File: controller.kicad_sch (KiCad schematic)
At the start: 26 parts, among them J5 Conn_01x10_Pin, J6 Conn_01x10_Pin, J8 AVR-ISP-6, Q1 BSS138, Q2 BSS138, Q3 BSS138, U10 ATmega328PB-A, Y1 16M

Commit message: weiter layoutet...
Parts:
- removed C14: 27p, symbol Device:C_Small
- removed J6: Conn_01x10_Pin, symbol Connector:Conn_01x10_Pin
- removed Q1, Q2, Q3: BSS138, Package_TO_SOT_SMD:SOT-23, symbol Transistor_FET:BSS138
- removed R11, R5, R7, R8: 1k, symbol Device:R_Small
- removed Y1: 16M, Crystal:Crystal_SMD_HC49-SD, symbol Device:Crystal_Small
- added C37, C46: 2u2, Capacitor_SMD:C_0805_2012Metric_Pad1.18x1.45mm_HandSolder, symbol Device:C_Small
- added C38, C39, C40: 100n, Capacitor_SMD:C_0805_2012Metric_Pad1.18x1.45mm_HandSolder, symbol Device:C_Small
- added D2: LED_Small, LED_SMD:LED_0805_2012Metric_Pad1.15x1.40mm_HandSolder, symbol Device:LED_Small
- added D6: SMAJ5.0CA, Diode_SMD:D_SMA, symbol Diode:SMAJ5.0CA
- added FB5, FB6: FerriteBead_Small, Inductor_SMD:L_0805_2012Metric_Pad1.15x1.40mm_HandSolder, symbol Device:FerriteBead_Small
- added FL1: Choke_Coilcraft_0603USB-251, Inductor_SMD:L_CommonModeChoke_Coilcraft_0603USB, symbol Filter:Choke_Coilcraft_0603USB-251
- added J10: Conn_01x06_Socket, Connector_PinHeader_2.54mm:PinHeader_1x06_P2.54mm_Vertical, symbol Connector:Conn_01x06_Socket
- added J6: Conn_01x06_Socket, Connector_PinHeader_2.54mm:PinHeader_1x06_P2.54mm_Horizontal, symbol Connector:Conn_01x06_Socket
- added J7: USB_B, Connector_USB:USB_B_Lumberg_2411_02_Horizontal, symbol Connector:USB_B
- added R14, R15: 33, Resistor_SMD:R_0805_2012Metric_Pad1.20x1.40mm_HandSolder, symbol Device:R_Small
- added SW1: SW_SP5T_NR01105, Button_Switch_THT:SW_NKK_NR01, symbol Switch:SW_SP5T_NR01105
- added U11: FT232RL, Package_SO:SSOP-28_5.3x10.2mm_P0.65mm, symbol Interface_USB:FT232RL
- added U12: WE-TVS-82400102, Package_TO_SOT_SMD:SOT-23-6, symbol Power_Protection:WE-TVS-82400102
- added Y1: ECS-2520MV-xxx-xx, Oscillator:Oscillator_SMD_ECS_2520MV-xxx-xx-4Pin_2.5x2.0mm, symbol Oscillator:ECS-2520MV-xxx-xx
- C12, C15, C16, C17, C18: footprint (none) -> Capacitor_SMD:C_0805_2012Metric_Pad1.18x1.45mm_HandSolder
- C13: value 27p -> 100n; footprint (none) -> Capacitor_SMD:C_0805_2012Metric_Pad1.18x1.45mm_HandSolder
- FB3: footprint Inductor_SMD:L_0805_2012Metric_Pad1.05x1.20mm_HandSolder -> Inductor_SMD:L_0805_2012Metric_Pad1.15x1.40mm_HandSolder
- J5: footprint (none) -> Connector_PinHeader_2.54mm:PinHeader_1x10_P2.54mm_Vertical
- J8: footprint Connector_IDC:IDC-Header_2x05_P2.54mm_Vertical -> Connector_IDC:IDC-Header_2x03_P2.54mm_Vertical
- R10, R6, R9: footprint (none) -> Resistor_SMD:R_0805_2012Metric_Pad1.20x1.40mm_HandSolder
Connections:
- net SDA_5 is gone; now on net SDA_3: TP1.1, U10.27 (PC4)
- net +3V3: now also FB3.1, J5.10 (Pin_10), J5.9 (Pin_9), J8.2 (VCC)
- net GND: now also C37.1, C38.1, C39.1, C40.1, C46.1, D2.1 (K), D6.1 (A1), J7.4 (GND), J7.5 (Shield), SW1.MP, U11.18 (GND), U11.21 (GND), U11.25 (AGND), U11.7 (GND), U12.2, Y1.1 (Tri-State), Y1.2 (GND)
- net INT_3: now also TP3.1, U10.26 (PC3)
- net RXD: now also U11.5 (RXD)
- net SCL_3: now also TP2.1, U10.28 (PC5)
- net TXD: now also U11.1 (TXD)
- net at U10.8 (XTAL2/PB7): no longer C13.2
- net at U10.1 (PD3): now also J10.2 (Pin_2), J6.2 (Pin_2), SW1.5
- net at U10.10 (PD6): now also J10.5 (Pin_5), J6.5 (Pin_5), SW1.2
- net at U10.11 (PD7): now also J10.6 (Pin_6), J6.6 (Pin_6), SW1.1
- net at U10.2 (PD4): now also J10.3 (Pin_3), J6.3 (Pin_3), SW1.4
- net at U10.3 (PE0): now also R9.2
- net at U10.32 (PD2): now also R10.1
- net at U10.7 (XTAL1/PB6): now also Y1.3 (OUT)
- net at U10.9 (PD5): now also J10.4 (Pin_4), J6.4 (Pin_4), SW1.3
- removed net +5VD: FB3.1, J5.10 (Pin_10), J5.9 (Pin_9), J8.2 (VCC), R10.1, R6.2, R9.1
- net 5VD_FIL renamed 3V3D_FIL
- net 3V3D_FIL: now also C13.2, R6.2, Y1.4 (VDD)
- removed net INT_5: R10.2, TP3.1, U10.26 (PC3)
- removed net SCL_5: R9.2, TP2.1, U10.28 (PC5)
- new net: FB6.1, J7.1 (VBUS)
- new net: FL1.4, J7.2 (D-)
- new net: FL1.1, J7.3 (D+)
- new net: FL1.3, U12.1
- new net: FL1.2, U12.3
- new net: J10.1 (Pin_1), J6.1 (Pin_1), R10.2, SW1.C (Common)
- new net: R15.2, U11.15 (USBD+)
- new net: R14.2, U11.16 (USBD-)
- new net: C39.2, C40.2, U11.17 (3V3OUT), U11.4 (VCCIO)
- new net: D2.2 (A), R9.1
- new net USB_D+: R15.1, U12.4
- new net USB_D-: R14.1, U12.6
- new net VBUS: C46.2, D6.2 (A2), FB5.1, FB6.2, U12.5
- new net VBUS_FIL: C37.2, C38.2, FB5.2, U11.19 (~{RESET}), U11.20 (VCC)
- no-connect marks 7 -> 21
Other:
- moved on the sheet: C12, C15, C16, C17, C18, J5, J8, R6, TP1, TP2, TP3, U10

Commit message: noch ein paar Kleinigkeiten
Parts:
- added C14, C51, C52, C53, C54: 100n, Capacitor_SMD:C_0805_2012Metric_Pad1.18x1.45mm_HandSolder, symbol Device:C_Small
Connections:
- net GND: now also C14.1, C51.1, C52.1, C53.1, C54.1
- net at J10.2 (Pin_2), J6.2 (Pin_2), SW1.5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: now also C54.2
- net at J10.5 (Pin_5), J6.5 (Pin_5), SW1.2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: now also C51.2
- net at J10.6 (Pin_6), J6.6 (Pin_6), SW1.1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: now also C14.2
- net at J10.3 (Pin_3), J6.3 (Pin_3), SW1.4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: now also C53.2
- net at J10.4 (Pin_4), J6.4 (Pin_4), SW1.3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: now also C52.2

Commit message: BOM angefangen und im Layout vom Hundertsten ins Tausendste gekommen...
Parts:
- C12, C13, C14, C15, C16, C38, C39, C40, C51, C52, C53, C54: Distributor (none) -> Mouser; Distributor PN (none) -> 581-KAM21BR71H104JT; Manufacturer (none) -> KYOCERA AVX; Manufacturer PN (none) -> KAM21BR71H104JT
- C17, C18, C37, C46: Distributor (none) -> Mouser; Distributor PN (none) -> 581-KAM21KR71E225KU; Manufacturer (none) -> KYOCERA AVX; Manufacturer PN (none) -> KAM21KR71E225KU
- D2: Distributor (none) -> Mouser; Distributor PN (none) -> 859-LTST-C171KGKT; Manufacturer (none) -> LITEON; Manufacturer PN (none) -> LTST-C171KGKT
- D6: Distributor (none) -> Mouser; Distributor PN (none) -> 576-SMAJ5.0CA; Manufacturer (none) -> Littelfuse; Manufacturer PN (none) -> SMAJ5.0CA
- FL1: Distributor (none) -> Mouser; Distributor PN (none) -> 994-0603USB-601MLC; Manufacturer (none) -> Coilcraft; Manufacturer PN (none) -> 0603USB-601MLC
- J5: now not fitted
- J7: Distributor PN (none) -> 200-USBBSFBTHFR; Manufacturer (none) -> Samtec; Manufacturer PN (none) -> USB-B-S-F-B-TH-FR
- J8: Distributor (none) -> Mouser; Distributor PN (none) -> 737-BHR-06-VUA; Manufacturer (none) -> Adam Tech; Manufacturer PN (none) -> BHR-06-VUA
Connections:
- net at C53.2, J10.3 (Pin_3), J6.3 (Pin_3)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: now also SW1.1; no longer SW1.4
- net at C14.2, J10.6 (Pin_6), J6.6 (Pin_6)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: now also SW1.3; no longer SW1.1
- net at C52.2, J10.4 (Pin_4), J6.4 (Pin_4)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: now also SW1.4; no longer SW1.3
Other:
- moved on the sheet: SW1

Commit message: es wird nicht besser... Beschriftungen und co. BOM angefangen...
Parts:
- added D5, D7: LED_Small, LED_SMD:LED_0805_2012Metric_Pad1.15x1.40mm_HandSolder, symbol Device:LED_Small
- added R11, R16: 1k, Resistor_SMD:R_0805_2012Metric_Pad1.20x1.40mm_HandSolder, symbol Device:R_Small
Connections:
- net GND: now also D5.1 (K), D7.1 (K)
- net at U11.22 (CBUS1): now also R16.2
- net at U11.23 (CBUS0): now also R11.2
- new net: D7.2 (A), R16.1
- new net: D5.2 (A), R11.1
- no-connect marks 21 -> 19

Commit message: BOM...
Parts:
- J10: Distributor (none) -> Mouser; Distributor PN (none) -> TC33X-2-103E; Manufacturer (none) -> Adam Tech; Manufacturer PN (none) -> PH1RB-06-UA
- J7: Distributor (none) -> Mouser
- SW1: Distributor (none) -> Mouser; Distributor PN (none) -> 633-NR01105ANG13-2A; Manufacturer (none) -> NKK Switches; Manufacturer PN (none) -> NR01105ANG13-2A
- U10: Distributor (none) -> Mouser; Distributor PN (none) -> 556-ATMEGA328PB-ANR; Manufacturer (none) -> Microchip Technology; Manufacturer PN (none) -> ATMEGA328PB-ANR
- U11: Distributor (none) -> Mouser; Distributor PN (none) -> 895-FT232RNL-TUBE; Manufacturer (none) -> FTDI; Manufacturer PN (none) -> FT232RNL-TUBE
- U12: Distributor (none) -> Mouser; Distributor PN (none) -> 710-82400102; Manufacturer (none) -> Wurth Elektronik; Manufacturer PN (none) -> 82400102
- Y1: Distributor (none) -> Mouser; Distributor PN (none) -> 520-2520MVLC080BNTR3; Manufacturer (none) -> ECS; Manufacturer PN (none) -> ECS-2520MVLC-080-BN-TR3
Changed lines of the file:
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@@
 			)
 		)
+		(property "Distributor" "Mouser"
+			(at 21.59 29.21 0)
+			(effects
+				(font
+					(size 1.27 1.27)
+				)
+			)
+		)
 		(pin "2"
 		)
@@
 			)
 		)
+		(property "Distributor" "Mouser"
+			(at 57.15 30.48 0)
+			(effects
+				(font
+					(size 1.27 1.27)
+				)
+			)
+		)
+		(property "Distributor PN" "710-82400102"
+			(at 57.15 30.48 0)
+			(effects
+				(font
+					(size 1.27 1.27)
+				)
+			)
+		)
+		(property "Manufacturer" "Wurth Elektronik"
+			(at 57.15 30.48 0)
+			(effects
+				(font
+					(size 1.27 1.27)
+				)
+			)
+		)
+		(property "Manufacturer PN" "82400102"
+			(at 57.15 30.48 0)
+			(effects
+				(font
+					(size 1.27 1.27)
+				)
+			)
+		)
 		(pin "5"
 		)
@@
 			)
 		)
-		(property "Manufacturer PN" ""
+		(property "Manufacturer PN" "ECS-2520MVLC-080-BN-TR3 "
 			(at 250.19 106.68 0)
 			(effects
@@
 			)
 		)
-		(property "Manufacturer" ""
+		(property "Manufacturer" "ECS"
 			(at 250.19 106.68 0)
 			(effects
@@
 			)
 		)
-		(property "Distributor" ""
+		(property "Distributor" "Mouser"
 			(at 250.19 106.68 0)
 			(effects
@@
 			)
 		)
-		(property "Distributor PN" ""
+		(property "Distributor PN" " 520-2520MVLC080BNTR3 "
 			(at 250.19 106.68 0)
 			(effects
@@
 			)
 		)
+		(property "Distributor" "Mouser"
+			(at 97.79 83.82 0)
+			(effects
+				(font
+					(size 1.27 1.27)
+				)
+			)
+		)
+		(property "Distributor PN" " 895-FT232RNL-TUBE "
+			(at 97.79 83.82 0)
+			(effects
+				(font
+					(size 1.27 1.27)
+				)
+			)
+		)
+		(property "Manufacturer" "FTDI"
+			(at 97.79 83.82 0)
+			(effects
+				(font
+					(size 1.27 1.27)
+				)
+			)
+		)
+		(property "Manufacturer PN" "FT232RNL-TUBE"
+			(at 97.79 83.82 0)
+			(effects
+				(font
+					(size 1.27 1.27)
+				)
+			)
+		)
 		(pin "21"
 		)
@@
 			)
 		)
+		(property "Distributor" "Mouser"
+			(at 179.07 115.57 0)
+			(effects
+				(font
+					(size 1.27 1.27)
+				)
+			)
+		)
+		(property "Distributor PN" " 556-ATMEGA328PB-ANR"
+			(at 179.07 115.57 0)
+			(effects
+				(font
+					(size 1.27 1.27)
+				)
+			)
+		)
+		(property "Manufacturer" "Microchip Technology "
+			(at 179.07 115.57 0)
+			(effects
+				(font
+					(size 1.27 1.27)
+				)
+			)
+		)
+		(property "Manufacturer PN" "ATMEGA328PB-ANR"
+			(at 179.07 115.57 0)
+			(effects
+				(font
+					(size 1.27 1.27)
+				)
+			)
+		)
 		(pin "5"
 		)
@@
 			)
 		)
-		(property "Manufacturer PN" ""
+		(property "Manufacturer PN" "PH1RB-06-UA"
 			(at 246.38 138.43 0)
 			(effects
@@
 			)
 		)
-		(property "Manufacturer" ""
+		(property "Manufacturer" "Adam Tech "
 			(at 246.38 138.43 0)
 			(effects
@@
 			)
 		)
-		(property "Distributor" ""
+		(property "Distributor" "Mouser"
 			(at 246.38 138.43 0)
 			(effects
@@
 			)
 		)
-		(property "Distributor PN" ""
+		(property "Distributor PN" "TC33X-2-103E"
 			(at 246.38 138.43 0)
 			(effects
@@
 			)
 		)
-		(property "Manufacturer PN" ""
+		(property "Manufacturer PN" "NR01105ANG13-2A"
 			(at 267.97 140.97 0)
 			(effects
@@
 			)
 		)
-		(property "Manufacturer" ""
+		(property "Manufacturer" "NKK Switches"
 			(at 267.97 140.97 0)
 			(effects
@@
 			)
 		)
-		(property "Distributor" ""
+		(property "Distributor" "Mouser"
 			(at 267.97 140.97 0)
 			(effects
@@
 			)
 		)
-		(property "Distributor PN" ""
+		(property "Distributor PN" "633-NR01105ANG13-2A"
 			(at 267.97 140.97 0)
 			(effects

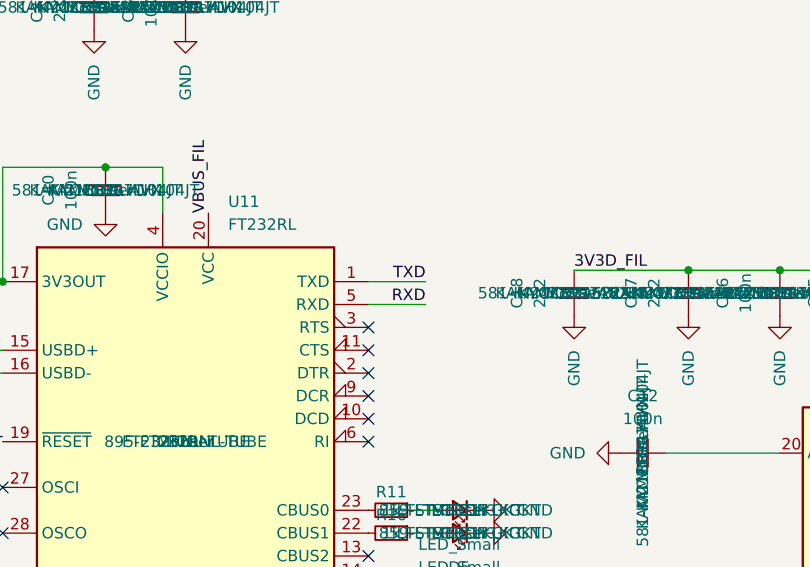
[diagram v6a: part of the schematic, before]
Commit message: Der Klassiker: RX und TX Leitungen vertauscht. Jetzt im Dutzend billiger. Korrigiert...
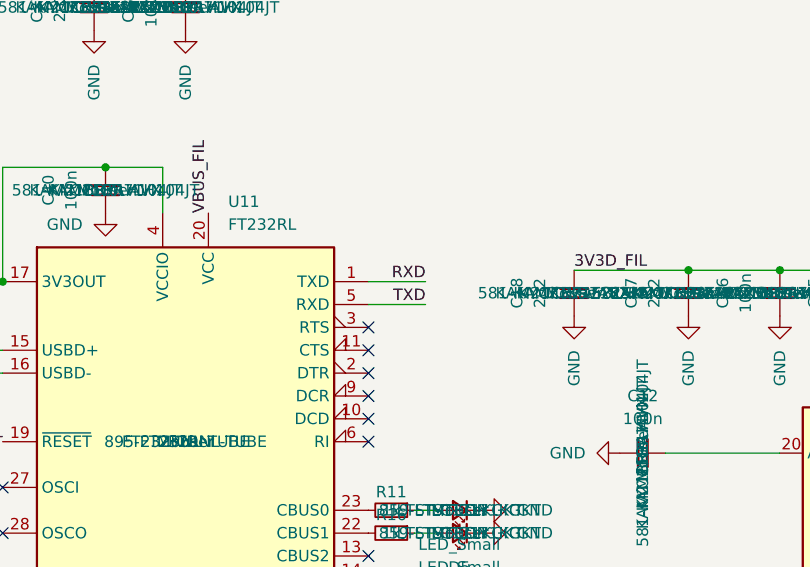
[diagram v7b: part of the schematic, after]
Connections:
- net RXD: now also U11.1 (TXD); no longer U11.5 (RXD)
- net TXD: now also U11.5 (RXD); no longer U11.1 (TXD)
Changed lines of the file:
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@@
 	)
 	(label "RXD"
-		(at 124.46 68.58 180)
+		(at 124.46 66.04 180)
 		(effects
 			(font
@@
 	)
 	(label "TXD"
-		(at 124.46 66.04 180)
+		(at 124.46 68.58 180)
 		(effects
 			(font
